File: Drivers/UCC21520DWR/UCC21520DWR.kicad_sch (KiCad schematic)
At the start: 19 parts, among them J1 Output, J3 Input, U1 UCC21520DWR

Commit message: UCC21520DWR
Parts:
- U1: JlcRotOffset (none) -> -90
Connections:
- net +15V: now also C4.1, U1.11 (VDDB)
- net PL: now also R6.2; no longer R5.2
- net at D1.2 (A), R2.2: no longer C4.1, U1.11 (VDDB)
- net at D3.1 (K): now also R5.2; no longer R6.2
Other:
- moved on the sheet: R5, R6
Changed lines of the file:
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@@
   (junction (at 189.23 109.22) (diameter 0) (color 0 0 0 0)
   )
+  (junction (at 157.48 106.68) (diameter 0) (color 0 0 0 0)
+  )
   (junction (at 213.36 106.68) (diameter 0) (color 0 0 0 0)
   )
-  (junction (at 157.48 74.93) (diameter 0) (color 0 0 0 0)
-  )
-  (junction (at 154.94 106.68) (diameter 0) (color 0 0 0 0)
-  )
   (wire (pts (xy 121.92 99.06) (xy 127 99.06))
     (stroke (width 0) (type default))
@@
     (stroke (width 0) (type default))
   )
-  (wire (pts (xy 154.94 74.93) (xy 157.48 74.93))
-    (stroke (width 0) (type default))
-  )
   (wire (pts (xy 121.92 101.6) (xy 127 101.6))
     (stroke (width 0) (type default))
@@
     (stroke (width 0) (type default))
   )
-  (wire (pts (xy 154.94 74.93) (xy 154.94 106.68))
-    (stroke (width 0) (type default))
-  )
   (wire (pts (xy 124.46 111.76) (xy 124.46 115.57))
     (stroke (width 0) (type default))
@@
     (stroke (width 0) (type default))
   )
-  (wire (pts (xy 157.48 74.93) (xy 157.48 76.2))
-    (stroke (width 0) (type default))
-  )
   (wire (pts (xy 189.23 106.68) (xy 193.04 106.68))
     (stroke (width 0) (type default))
@@
     (stroke (width 0) (type default))
   )
+  (wire (pts (xy 157.48 106.68) (xy 162.56 106.68))
+    (stroke (width 0) (type default))
+  )
   (wire (pts (xy 217.17 119.38) (xy 173.99 119.38))
     (stroke (width 0) (type default))
   )
-  (wire (pts (xy 154.94 106.68) (xy 162.56 106.68))
+  (wire (pts (xy 152.4 106.68) (xy 157.48 106.68))
     (stroke (width 0) (type default))
   )
@@
     (stroke (width 0) (type default))
   )
-  (wire (pts (xy 152.4 106.68) (xy 154.94 106.68))
-    (stroke (width 0) (type default))
-  )
   (wire (pts (xy 170.18 106.68) (xy 173.99 106.68))
     (stroke (width 0) (type default))
@@
     (stroke (width 0) (type default))
   )
-  (wire (pts (xy 157.48 73.66) (xy 157.48 74.93))
+  (wire (pts (xy 157.48 73.66) (xy 157.48 76.2))
     (stroke (width 0) (type default))
   )
@@
   )
   (wire (pts (xy 95.25 121.92) (xy 91.44 121.92))
+    (stroke (width 0) (type default))
+  )
+  (wire (pts (xy 157.48 100.965) (xy 157.48 106.68))
     (stroke (width 0) (type default))
   )
@@
     )
   )
-  (symbol (lib_id "Device:R") (at 196.85 113.03 90) (unit 1)
+  (symbol (lib_id "Device:R") (at 196.85 106.68 90) (unit 1)
     (in_bom yes) (on_board yes) (dnp no)
-    (property "Reference" "R6" (at 196.85 110.49 90)
-      (effects (font (size 1.27 1.27)))
-    )
-    (property "Value" "2r2" (at 196.85 113.03 90)
-      (effects (font (size 1.27 1.27)))
-    )
-    (property "Footprint" "Resistor_SMD:R_0805_2012Metric" (at 196.85 114.808 90)
-      (effects (font (size 1.27 1.27)) hide)
-    )
-    (property "Datasheet" "~" (at 196.85 113.03 0)
+    (property "Reference" "R6" (at 196.85 104.14 90)
+      (effects (font (size 1.27 1.27)))
+    )
+    (property "Value" "2r2" (at 196.85 106.68 90)
+      (effects (font (size 1.27 1.27)))
+    )
+    (property "Footprint" "Resistor_SMD:R_0805_2012Metric" (at 196.85 108.458 90)
+      (effects (font (size 1.27 1.27)) hide)
+    )
+    (property "Datasheet" "~" (at 196.85 106.68 0)
       (effects (font (size 1.27 1.27)) hide)
     )
@@
     )
     (property "MPN" "C601651" (at 139.7 101.6 0)
+      (effects (font (size 1.27 1.27)) hide)
+    )
+    (property "JlcRotOffset" "-90" (at 139.7 101.6 0)
       (effects (font (size 1.27 1.27)) hide)
     )
@@
     )
   )
-  (symbol (lib_id "Device:R") (at 196.85 106.68 90) (unit 1)
+  (symbol (lib_id "Device:R") (at 196.85 113.03 90) (unit 1)
     (in_bom yes) (on_board yes) (dnp no)
-    (property "Reference" "R5" (at 196.85 104.14 90)
-      (effects (font (size 1.27 1.27)))
-    )
-    (property "Value" "2r2" (at 196.85 106.68 90)
-      (effects (font (size 1.27 1.27)))
-    )
-    (property "Footprint" "Resistor_SMD:R_0805_2012Metric" (at 196.85 108.458 90)
-      (effects (font (size 1.27 1.27)) hide)
-    )
-    (property "Datasheet" "~" (at 196.85 106.68 0)
+    (property "Reference" "R5" (at 196.85 110.49 90)
+      (effects (font (size 1.27 1.27)))
+    )
+    (property "Value" "2r2" (at 196.85 113.03 90)
+      (effects (font (size 1.27 1.27)))
+    )
+    (property "Footprint" "Resistor_SMD:R_0805_2012Metric" (at 196.85 114.808 90)
+      (effects (font (size 1.27 1.27)) hide)
+    )
+    (property "Datasheet" "~" (at 196.85 113.03 0)
       (effects (font (size 1.27 1.27)) hide)
     )
@@
         )
       )
+    )
+  )
+  (symbol (lib_id "power:+15V") (at 157.48 100.965 0) (unit 1)
+    (in_bom yes) (on_board yes) (dnp no)
+    (property "Reference" "#PWR08" (at 157.48 104.775 0)
+      (effects (font (size 1.27 1.27)) hide)
+    )
+    (property "Value" "+15V" (at 161.29 99.695 0)
+      (effects (font (size 1.27 1.27)))
+    )
+    (property "Footprint" "" (at 157.48 100.965 0)
+      (effects (font (size 1.27 1.27)) hide)
+    )
+    (property "Datasheet" "" (at 157.48 100.965 0)
+      (effects (font (size 1.27 1.27)) hide)
+    )
+    (pin "1")
+    (instances
+      (project "UCC21520DWR"
+        (path "/21ffef13-51c1-4f75-9c5e-4fb42baba5c7"
+          (reference "#PWR08") (unit 1)
+        )
+      )
+      (project "GigaVescDrivers"
+        (path "/74b7e1db-46d0-4e07-8500-01cfc2fa8362/60c370e3-7758-4e46-877e-f687e0b59f6d"
+          (reference "#PWR024") (unit 1)
+        )
+        (path "/74b7e1db-46d0-4e07-8500-01cfc2fa8362/087677ba-107a-4510-bc80-02c4cece2e63"
+          (reference "#PWR038") (unit 1)
+        )
+        (path "/74b7e1db-46d0-4e07-8500-01cfc2fa8362/76b34049-053a-4f0a-90ce-743149c2c6b2"
+          (reference "#PWR051") (unit 1)
+        )
+      )

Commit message: organization
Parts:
- added TP1, TP2: TestPoint, TestPoint:TestPoint_Pad_D1.0mm, symbol Connector:TestPoint
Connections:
- net at R3.1, R4.1, U1.15 (OUTA): now also TP1.1
- net at R5.1, R6.1, U1.10 (OUTB): now also TP2.1
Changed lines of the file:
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@@
   (junction (at 116.84 91.44) (diameter 0) (color 0 0 0 0)
   )
+  (junction (at 179.705 93.98) (diameter 0) (color 0 0 0 0)
+  )
   (junction (at 213.36 83.82) (diameter 0) (color 0 0 0 0)
   )
@@
   (junction (at 173.99 111.76) (diameter 0) (color 0 0 0 0)
   )
+  (junction (at 179.705 109.22) (diameter 0) (color 0 0 0 0)
+  )
   (junction (at 217.17 106.68) (diameter 0) (color 0 0 0 0)
   )
@@
     (stroke (width 0) (type default))
   )
-  (wire (pts (xy 152.4 93.98) (xy 181.61 93.98))
+  (wire (pts (xy 152.4 93.98) (xy 179.705 93.98))
     (stroke (width 0) (type default))
   )
@@
     (stroke (width 0) (type default))
   )
+  (wire (pts (xy 179.705 93.98) (xy 181.61 93.98))
+    (stroke (width 0) (type default))
+  )
   (wire (pts (xy 189.23 113.03) (xy 193.04 113.03))
     (stroke (width 0) (type default))
@@
     (stroke (width 0) (type default))
   )
-  (wire (pts (xy 152.4 109.22) (xy 189.23 109.22))
+  (wire (pts (xy 152.4 109.22) (xy 179.705 109.22))
     (stroke (width 0) (type default))
   )
@@
   )
   (wire (pts (xy 85.09 118.11) (xy 85.09 121.92))
+    (stroke (width 0) (type default))
+  )
+  (wire (pts (xy 179.705 109.22) (xy 189.23 109.22))
     (stroke (width 0) (type default))
   )
@@
   (symbol (lib_id "Device:C") (at 166.37 106.68 90) (unit 1)
     (in_bom yes) (on_board yes) (dnp no)
-    (property "Reference" "C4" (at 166.37 102.87 90)
-      (effects (font (size 1.27 1.27)))
-    )
-    (property "Value" "4.7u 50v" (at 173.355 104.775 90)
+    (property "Reference" "C4" (at 163.195 104.775 90)
+      (effects (font (size 1.27 1.27)))
+    )
+    (property "Value" "4.7u 50v" (at 168.275 102.87 90)
       (effects (font (size 1.27 1.27)))
     )
@@
       (effects (font (size 1.27 1.27)))
     )
-    (property "Value" "4.7u 50v" (at 173.99 89.535 90)
+    (property "Value" "4.7u 50v" (at 168.275 86.995 90)
       (effects (font (size 1.27 1.27)))
     )
@@
         (path "/74b7e1db-46d0-4e07-8500-01cfc2fa8362/76b34049-053a-4f0a-90ce-743149c2c6b2"
           (reference "#PWR045") (unit 1)
+        )
+      )
+    )
+  )
+  (symbol (lib_id "Connector:TestPoint") (at 179.705 109.22 0) (unit 1)
+    (in_bom yes) (on_board yes) (dnp no)
+    (property "Reference" "TP2" (at 181.61 106.68 0)
+      (effects (font (size 1.27 1.27)) (justify left))
+    )
+    (property "Value" "TestPoint" (at 176.53 103.505 0)
+      (effects (font (size 1.27 1.27)) (justify left))
+    )
+    (property "Footprint" "TestPoint:TestPoint_Pad_D1.0mm" (at 184.785 109.22 0)
+      (effects (font (size 1.27 1.27)) hide)
+    )
+    (property "Datasheet" "~" (at 184.785 109.22 0)
+      (effects (font (size 1.27 1.27)) hide)
+    )
+    (pin "1")
+    (instances
+      (project "UCC21520DWR"
+        (path "/21ffef13-51c1-4f75-9c5e-4fb42baba5c7"
+          (reference "TP2") (unit 1)
         )
       )
@@
         )
       )
+    )
+  )
+  (symbol (lib_id "Connector:TestPoint") (at 179.705 93.98 0) (unit 1)
+    (in_bom yes) (on_board yes) (dnp no)
+    (property "Reference" "TP1" (at 182.88 92.075 0)
+      (effects (font (size 1.27 1.27)) (justify left))
+    )
+    (property "Value" "TestPoint" (at 175.26 87.63 0)
+      (effects (font (size 1.27 1.27)) (justify left))
+    )
+    (property "Footprint" "TestPoint:TestPoint_Pad_D1.0mm" (at 184.785 93.98 0)
+      (effects (font (size 1.27 1.27)) hide)
+    )
+    (property "Datasheet" "~" (at 184.785 93.98 0)
+      (effects (font (size 1.27 1.27)) hide)
+    )
+    (pin "1")
+    (instances
+      (project "UCC21520DWR"
+        (path "/21ffef13-51c1-4f75-9c5e-4fb42baba5c7"
+          (reference "TP1") (unit 1)
+        )
+      )

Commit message: new_format
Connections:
- net PHASE: now also J1.3 (Pin_3); no longer J1.2 (Pin_2)
- net PHASE_GROUND: now also J1.4 (Pin_4); no longer J1.3 (Pin_3)
- net PL: now also J1.2 (Pin_2); no longer J1.4 (Pin_4)
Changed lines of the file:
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@@
     (effects (font (size 1.27 1.27)) (justify right))
   )
-  (hierarchical_label "PHASE_GROUND" (shape input) (at 255.27 96.52 180) (fields_autoplaced)
+  (hierarchical_label "PHASE_GROUND" (shape input) (at 255.27 99.06 180) (fields_autoplaced)
     (effects (font (size 1.27 1.27)) (justify right))
   )
@@
     (effects (font (size 1.27 1.27)) (justify right))
   )
-  (hierarchical_label "PL" (shape input) (at 255.27 99.06 180) (fields_autoplaced)
+  (hierarchical_label "PL" (shape input) (at 255.27 93.98 180) (fields_autoplaced)
     (effects (font (size 1.27 1.27)) (justify right))
   )
-  (hierarchical_label "PHASE" (shape input) (at 255.27 93.98 180) (fields_autoplaced)
+  (hierarchical_label "PHASE" (shape input) (at 255.27 96.52 180) (fields_autoplaced)
     (effects (font (size 1.27 1.27)) (justify right))
   )

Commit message: shunts
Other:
- moved on the sheet: TP1, TP2

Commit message: nearlyready
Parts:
- C1: Mouser (none) -> 80-T491D476K25AT7280
- C2, C5: MPN (none) -> C28233; Mouser (none) -> 187-CL21B104KBFNNNE
- C3, C4: Mouser (none) -> 81-GRM319R61H475KA2D
- D1: Mouser (none) -> 750-SS520B-HF
- D2: MPN (none) -> C511866; Mouser (none) -> 621-SBR3U40S1FQ-7
- D3: Mouser (none) -> 621-SBR3U40S1FQ-7
- R1: Mouser (none) -> 71-CRCW0805J-20K-E3
- R2: Mouser (none) -> 603-RC0805JR-072R2L
- R3, R4, R5, R6: MPN (none) -> C17521; Mouser (none) -> 603-RC0805JR-072R2L
- R7: Mouser (none) -> 603-RC0805FR-074K7L
- R8: MPN (none) -> C17673; Mouser (none) -> 603-RC0805FR-074K7L
- U1: Mouser (none) -> 595-UCC21520DWR
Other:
- note added: "Or any shottky diode with 200V 5A <850mV forward voltage"
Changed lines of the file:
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@@
     (stroke (width 0) (type default))
+  )
+  (text "Or any shottky diode with \n200V 5A\n<850mV forward voltage"
+    (at 130.81 80.01 0)
+    (effects (font (size 1.27 1.27)) (justify left bottom))
   )
   (hierarchical_label "PH" (shape input) (at 255.27 91.44 180) (fields_autoplaced)
@@
       (effects (font (size 1.27 1.27)) hide)
     )
+    (property "Mouser" "71-CRCW0805J-20K-E3" (at 85.09 114.3 0)
+      (effects (font (size 1.27 1.27)) hide)
+    )
     (pin "1")
     (pin "2")
@@
       (effects (font (size 1.27 1.27)) hide)
     )
+    (property "Mouser" "187-CL21B104KBFNNNE" (at 95.25 114.3 0)
+      (effects (font (size 1.27 1.27)) hide)
+    )
+    (property "MPN" "C28233" (at 95.25 114.3 0)
+      (effects (font (size 1.27 1.27)) hide)
+    )
     (pin "1")
     (pin "2")
@@
       (effects (font (size 1.27 1.27)) hide)
     )
+    (property "Mouser" "603-RC0805JR-072R2L" (at 196.85 90.17 0)
+      (effects (font (size 1.27 1.27)) hide)
+    )
+    (property "MPN" "C17521" (at 196.85 90.17 0)
+      (effects (font (size 1.27 1.27)) hide)
+    )
     (pin "1")
     (pin "2")
@@
       (effects (font (size 1.27 1.27)) hide)
     )
+    (property "Mouser" "81-GRM319R61H475KA2D" (at 166.37 106.68 0)
+      (effects (font (size 1.27 1.27)) hide)
+    )
     (pin "1")
     (pin "2")
@@
     )
     (property "MPN" "C17673" (at 217.17 87.63 90)
+      (effects (font (size 1.27 1.27)) hide)
+    )
+    (property "Mouser" "603-RC0805FR-074K7L" (at 217.17 87.63 0)
       (effects (font (size 1.27 1.27)) hide)
     )
@@
       (effects (font (size 1.27 1.27)) hide)
     )
+    (property "Mouser" "750-SS520B-HF" (at 157.48 80.01 0)
+      (effects (font (size 1.27 1.27)) hide)
+    )
     (pin "1")
     (pin "2")
@@
       (effects (font (size 1.27 1.27)) hide)
     )
+    (property "Mouser" "81-GRM319R61H475KA2D" (at 166.37 91.44 0)
+      (effects (font (size 1.27 1.27)) hide)
+    )
     (pin "1")
     (pin "2")
@@
       (effects (font (size 1.27 1.27)) hide)
     )
+    (property "Mouser" "" (at 180.34 109.22 0)
+      (effects (font (size 1.27 1.27)) hide)
+    )
     (pin "1")
     (instances
@@
       (effects (font (size 1.27 1.27)) hide)
     )
+    (property "Mouser" "187-CL21B104KBFNNNE" (at 111.76 95.25 0)
+      (effects (font (size 1.27 1.27)) hide)
+    )
+    (property "MPN" "C28233" (at 111.76 95.25 0)
+      (effects (font (size 1.27 1.27)) hide)
+    )
     (pin "1")
     (pin "2")
@@
       (effects (font (size 1.27 1.27)) hide)
     )
+    (property "Mouser" "603-RC0805JR-072R2L" (at 196.85 106.68 0)
+      (effects (font (size 1.27 1.27)) hide)
+    )
+    (property "MPN" "C17521" (at 196.85 106.68 0)
+      (effects (font (size 1.27 1.27)) hide)
+    )
     (pin "1")
     (pin "2")
@@
       (effects (font (size 1.27 1.27)) hide)
     )
+    (property "Mouser" "603-RC0805JR-072R2L" (at 196.85 83.82 0)
+      (effects (font (size 1.27 1.27)) hide)
+    )
+    (property "MPN" "C17521" (at 196.85 83.82 0)
+      (effects (font (size 1.27 1.27)) hide)
+    )
     (pin "1")
     (pin "2")
@@
       (effects (font (size 1.27 1.27)) hide)
     )
+    (property "Mouser" "621-SBR3U40S1FQ-7" (at 209.55 113.03 0)
+      (effects (font (size 1.27 1.27)) hide)
+    )
     (pin "1")
     (pin "2")
@@
     )
     (property "JlcRotOffset" "-90" (at 139.7 101.6 0)
+      (effects (font (size 1.27 1.27)) hide)
+    )
+    (property "Mouser" "595-UCC21520DWR" (at 139.7 101.6 0)
       (effects (font (size 1.27 1.27)) hide)
     )
@@
       (effects (font (size 1.27 1.27)) hide)
     )
+    (property "Mouser" "" (at 260.35 93.98 0)
+      (effects (font (size 1.27 1.27)) hide)
+    )
     (pin "1")
     (pin "2")
@@
     )
     (property "Datasheet" "~" (at 33.02 100.33 0)
+      (effects (font (size 1.27 1.27)) hide)
+    )
+    (property "Mouser" "" (at 33.02 100.33 0)
       (effects (font (size 1.27 1.27)) hide)
     )
@@
       (effects (font (size 1.27 1.27)) hide)
     )
+    (property "Mouser" "" (at 177.8 91.44 0)
+      (effects (font (size 1.27 1.27)) hide)
+    )
     (pin "1")
     (instances
@@
       (effects (font (size 1.27 1.27)) hide)
     )
+    (property "Mouser" "603-RC0805JR-072R2L" (at 157.48 69.85 0)
+      (effects (font (size 1.27 1.27)) hide)
+    )
     (pin "1")
     (pin "2")
@@
       (effects (font (size 1.27 1.27)) hide)
     )
+    (property "Mouser" "603-RC0805JR-072R2L" (at 196.85 113.03 0)
+      (effects (font (size 1.27 1.27)) hide)
+    )
+    (property "MPN" "C17521" (at 196.85 113.03 0)
+      (effects (font (size 1.27 1.27)) hide)
+    )
     (pin "1")
     (pin "2")
@@
       (effects (font (size 1.27 1.27)) hide)
     )
+    (property "Mouser" "621-SBR3U40S1FQ-7" (at 209.55 83.82 0)
+      (effects (font (size 1.27 1.27)) hide)
+    )
+    (property "MPN" "C511866" (at 209.55 83.82 0)
+      (effects (font (size 1.27 1.27)) hide)
+    )
     (pin "1")
     (pin "2")
@@
       (effects (font (size 1.27 1.27)) hide)
     )
+    (property "Mouser" "603-RC0805FR-074K7L" (at 217.17 110.49 0)
+      (effects (font (size 1.27 1.27)) hide)
+    )
+    (property "MPN" "C17673" (at 217.17 110.49 0)
+      (effects (font (size 1.27 1.27)) hide)
+    )
     (pin "1")
     (pin "2")
@@
       (effects (font (size 1.27 1.27)) hide)
     )
+    (property "Mouser" "80-T491D476K25AT7280" (at 77.47 77.47 0)
+      (effects (font (size 1.27 1.27)) hide)
+    )

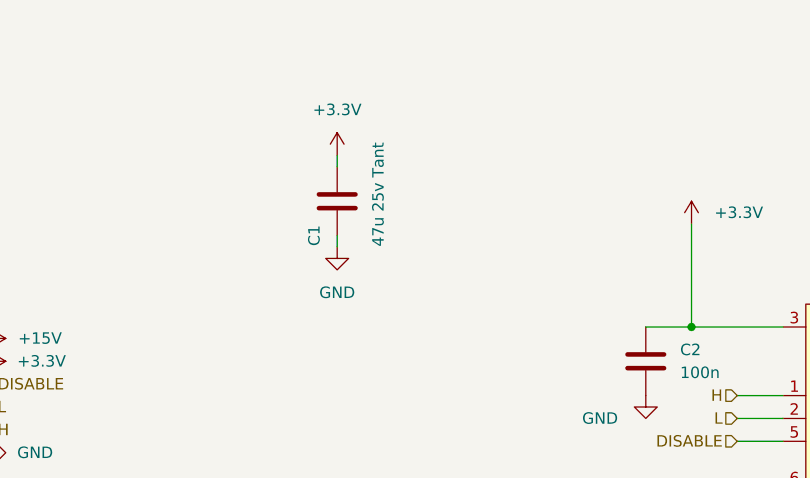
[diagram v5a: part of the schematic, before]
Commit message: fixes to caps
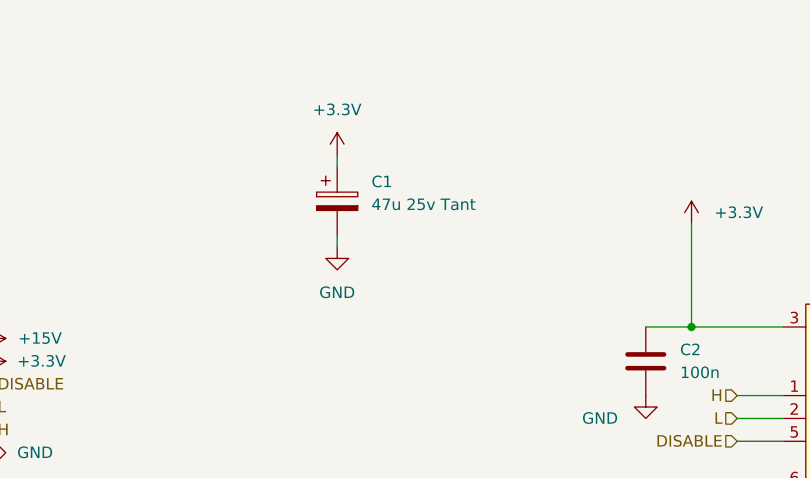
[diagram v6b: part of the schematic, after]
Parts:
- removed C1: 47u 25v Tant, Capacitor_Tantalum_SMD:CP_EIA-7343-31_Kemet-D, symbol Device:C
- added C1: 47u 25v Tant, Capacitor_Tantalum_SMD:CP_EIA-7343-31_Kemet-D, symbol Device:C_Polarized
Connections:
- net +3.3V: now also C1.1
- net GND: now also C1.2
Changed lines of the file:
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@@
+    )
+  )
+  (symbol (lib_id "Device:C_Polarized") (at 77.47 77.47 0) (unit 1)
+    (in_bom yes) (on_board yes) (dnp no) (fields_autoplaced)
+    (property "Reference" "C1" (at 81.28 75.311 0)
+      (effects (font (size 1.27 1.27)) (justify left))
+    )
+    (property "Value" "47u 25v Tant" (at 81.28 77.851 0)
+      (effects (font (size 1.27 1.27)) (justify left))
+    )
+    (property "Footprint" "Capacitor_Tantalum_SMD:CP_EIA-7343-31_Kemet-D" (at 78.4352 81.28 0)
+      (effects (font (size 1.27 1.27)) hide)
+    )
+    (property "Datasheet" "~" (at 77.47 77.47 0)
+      (effects (font (size 1.27 1.27)) hide)
+    )
+    (property "MPN" "C117039" (at 77.47 77.47 0)
+      (effects (font (size 1.27 1.27)) hide)
+    )
+    (pin "1")
+    (pin "2")
+    (instances
+      (project "UCC21520DWR"
+        (path "/21ffef13-51c1-4f75-9c5e-4fb42baba5c7"
+          (reference "C1") (unit 1)
+        )
+      )
     )
   )
@@
         )
       )
-    )
-  )
-  (symbol (lib_id "Device:C") (at 77.47 77.47 180) (unit 1)
-    (in_bom yes) (on_board yes) (dnp no)
-    (property "Reference" "C1" (at 74.93 81.28 90)
-      (effects (font (size 1.27 1.27)))
-    )
-    (property "Value" "47u 25v Tant" (at 82.042 76.708 90)
-      (effects (font (size 1.27 1.27)))
-    )
-    (property "Footprint" "Capacitor_Tantalum_SMD:CP_EIA-7343-31_Kemet-D" (at 76.5048 73.66 0)
-      (effects (font (size 1.27 1.27)) hide)
-    )
-    (property "Datasheet" "~" (at 77.47 77.47 0)
-      (effects (font (size 1.27 1.27)) hide)
-    )
-    (property "MPN" "C117039" (at 77.47 77.47 90)
-      (effects (font (size 1.27 1.27)) hide)
-    )
-    (property "Mouser" "80-T491D476K25AT7280" (at 77.47 77.47 0)
-      (effects (font (size 1.27 1.27)) hide)
-    )
-    (pin "1")
-    (pin "2")
-    (instances
-      (project "UCC21520DWR"
-        (path "/21ffef13-51c1-4f75-9c5e-4fb42baba5c7"
-          (reference "C1") (unit 1)
-        )
-      )
-      (project "GigaVescDrivers"
-        (path "/74b7e1db-46d0-4e07-8500-01cfc2fa8362/60c370e3-7758-4e46-877e-f687e0b59f6d"
-          (reference "C14") (unit 1)
-        )
-        (path "/74b7e1db-46d0-4e07-8500-01cfc2fa8362/087677ba-107a-4510-bc80-02c4cece2e63"
-          (reference "C18") (unit 1)
-        )
-        (path "/74b7e1db-46d0-4e07-8500-01cfc2fa8362/76b34049-053a-4f0a-90ce-743149c2c6b2"
-          (reference "C19") (unit 1)
-        )
-      )
